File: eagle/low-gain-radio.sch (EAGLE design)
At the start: 132 parts, among them U1 MKW01Z128, U2 SKY65116, U3 W25Q80DV, U4 LP5907MFX-3.3, U6 LP5907MFX-3.3, U7 LD39200, U8 MAAL-010704, Y1 32MHz

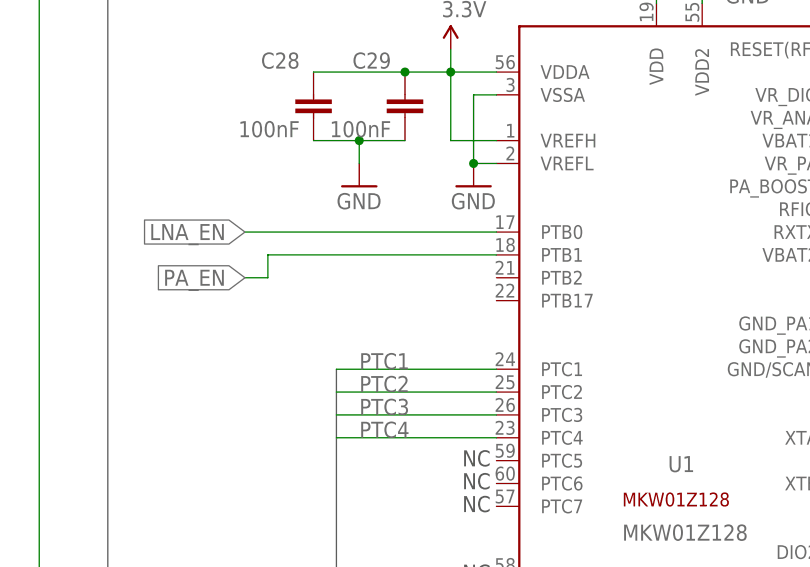
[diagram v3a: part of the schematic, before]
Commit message: added test points to PTB17, PTB2 and placed on PCB layout...also cleared a few stupid DRC errors on the PCB layout
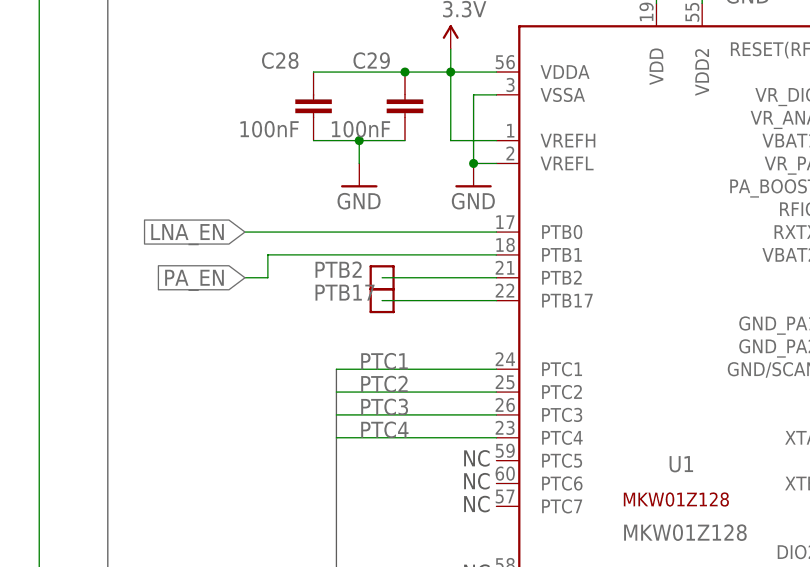
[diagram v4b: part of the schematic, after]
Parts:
- added PTB17, PTB2: TEST-POINT, Tova:TEST-POINT
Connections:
- new net PTB17: PTB17.1, U1.PTB17
- new net PTB2: PTB2.1, U1.PTB2
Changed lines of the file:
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@@
 <setting verticaltext="up"/>
 </settings>
-<grid distance="0.1" unitdist="inch" unit="inch" style="lines" multiple="1" display="yes" altdistance="0.01" altunitdist="inch" altunit="inch"/>
+<grid distance="0.1" unitdist="inch" unit="inch" style="lines" multiple="1" display="no" altdistance="0.01" altunitdist="inch" altunit="inch"/>
 <layers>
 <layer number="1" name="Top" color="4" fill="1" visible="no" active="no"/>
@@
 <attribute name="MPN" value="CBR04C101F3GAC"/>
 </part>
+<part name="PTB2" library="Tova" deviceset="TEST-POINT" device=""/>
+<part name="PTB17" library="Tova" deviceset="TEST-POINT" device=""/>
 </parts>
 <sheets>
@@
 <attribute name="MPN" x="530.86" y="190.5" size="1.778" layer="96" rot="R90" display="off"/>
 </instance>
+<instance part="PTB2" gate="G$1" x="81.28" y="220.98" smashed="yes">
+<attribute name="NAME" x="73.66" y="220.98" size="1.778" layer="95" font="vector"/>
+</instance>
+<instance part="PTB17" gate="G$1" x="81.28" y="218.44" smashed="yes">
+<attribute name="NAME" x="73.66" y="218.44" size="1.778" layer="95" font="vector"/>
+</instance>
 </instances>
 <busses>
@@
 </segment>
 </net>
+<net name="PTB2" class="0">
+<segment>
+<pinref part="U1" gate="G$1" pin="PTB2"/>
+<pinref part="PTB2" gate="G$1" pin="1"/>
+<wire x1="81.28" y1="220.98" x2="93.98" y2="220.98" width="0.1524" layer="91"/>
+</segment>
+</net>
+<net name="PTB17" class="0">
+<segment>
+<pinref part="U1" gate="G$1" pin="PTB17"/>
+<pinref part="PTB17" gate="G$1" pin="1"/>
+<wire x1="81.28" y1="218.44" x2="93.98" y2="218.44" width="0.1524" layer="91"/>
+</segment>
+</net>

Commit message: Big cleanup of v2_0 board. Includes changes to packages for LDOs and switch and reflectometer, ground stapling, adding a RGB LED, new board outline from rev 0.4 structure drawings, etc. Ready for production, except for possible switch to 0402s.
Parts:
- removed LED8: DNP/AMB, psas_c3_team05:LED-0603
- removed PTB17, PTB2: TEST-POINT, Tova:TEST-POINT
- removed U$22: BDCN-20-13+, low-gain-radio:BDCN-20-13+
- removed U$49: RF3025, low-gain-radio:RF3025
- added C59, C62: DNP, rcl_custom:C-EU0603-B-NOSILK
- added C63: 100pF, low-gain-radio:C-EU0402-C-NOSILK
- added LED9: SMLVN6RGB1W1, apdm:LED-RGB-SEPARATE-3528
- added R22, R23: DNP/1k, rcl_custom:R-US_0603-B-NOSILK
- added U5: RF3025, low-gain-radio:RF3025
- added U9: BDCN-20-13+, low-gain-radio:BDCN-20-13+
- added X0: DNP, microbuilder:CRYSTAL2.5X2.0MM
- added XTAL0: TEST-POINT, Tova:TEST-POINT
- renumbered XTAL to XTAL1, Y1 to X1
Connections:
- removed net DIO5/CLKOUT: DIO5/CLKOUT.1, U1.DIO5, U1.PTA18/EXTAL0
- new net EXTAL0: C62.2, DIO5/CLKOUT.1, U1.DIO5, U1.PTA18/EXTAL0, X0.1
- new net N$11: LED9B.K, R23.1
- new net N$26: LED9R.K, R12.1
- new net XTAL0: C59.2, U1.PTA19/XTAL0, X0.2, XTAL0.1
- net 3.3V: now also LED9B.A, LED9G.A, LED9R.A
- net DC_OUT: now also U9.OUT; no longer U$22.OUT
- net FWD: now also U9.FWD; no longer U$22.FWD
- net GND: now also C59.1, C62.1; no longer LED8.K
- net LNA_IN: now also U5.RF2; no longer U$49.RF2
- net N$23: now also LED9G.K, R22.1; no longer LED8.A, R12.1
- net PA_IN: now also U5.RF1; no longer U$49.RF1
- net PTA4/NMI_B: now also CF1.19, CF1.20; no longer CF1.2
- net PTB17: now also R23.2; no longer PTB17.1
- net PTB2: now also R22.2; no longer PTB2.1
- net REV: now also U9.REV; no longer U$22.REV
- net RFC: now also U9.IN; no longer U$22.IN
- net RF_GND: now also C63.1, U5.GND, U9.GND, U9.GND2; no longer U$22.GND, U$22.GND2, U$49.GND, U$49.GND1, U$49.GND10, U$49.GND2, U$49.GND3, U$49.GND4, U$49.GND5, U$49.GND6, U$49.GND7, U$49.GND8, U$49.GND9, U$49.PADDLE
- net RXTX: now also U5.VC; no longer U$49.VC
- net RXTX_OUT: now also U5.RFC; no longer U$49.RFC
- net UART0_RX: now also CF1.23, CF1.24; no longer CF1.17, CF1.18
- net UART0_TX: now also CF1.21, CF1.22; no longer CF1.15, CF1.16
- net VBIAS: now also C63.2, U5.VDD; no longer U$49.VDD
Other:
- note added: "CAN"
- note added: "MMCX to Antenna"
- note added: "Vpv"
- note removed: "GND lines for RF2 and RF3 need to go along their respective transmission lines to prevent intereference from other signals. I have left them this way though to conserve space."
- note removed: "MCX to 70 cm Antenna"
- moved on the sheet: C39, C40, C41, C42, C49, C52, C53, C55, C56, C57, C58, C60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

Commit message: did a sanity check everything looks good, added some missing attributes to parts on the schematic and changed some text on the board layout
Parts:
- LED9: DIST (none) -> Digi-Key Inc.; DPN (none) -> 846-1187-1-ND; MFG (none) -> Rohm Semiconductor; MPN (none) -> SMLVN6RGB1W1
- U2: DIST (none) -> Digi-Key Inc.; DPN (none) -> 863-1072-1-ND; MFG (none) -> Skyworks Solutions Inc.; MPN (none) -> SKY65116-21
- U5: DIST (none) -> Digi-Key Inc.; DPN (none) -> 689-1087-1-ND; MFG (none) -> RFMD; MPN (none) -> RF3025TR7
- U8: DIST (none) -> Digi-Key Inc.; DPN (none) -> 1465-1261-1-ND; MFG (none) -> M/A-Com Technology Solutions; MPN (none) -> MAAL-010704-TR3000
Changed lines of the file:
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@@
 <?xml version="1.0" encoding="utf-8"?>
 <!DOCTYPE eagle SYSTEM "eagle.dtd">
-<eagle version="7.5.0">
+<eagle version="7.3.0">
 <drawing>
 <settings>
@@
 <setting verticaltext="up"/>
 </settings>
-<grid distance="0.05" unitdist="inch" unit="inch" style="lines" multiple="1" display="no" altdistance="0.01" altunitdist="inch" altunit="inch"/>
+<grid distance="0.1" unitdist="inch" unit="inch" style="lines" multiple="1" display="no" altdistance="0.01" altunitdist="inch" altunit="inch"/>
 <layers>
 <layer number="1" name="Top" color="4" fill="1" visible="no" active="no"/>
@@
 <part name="DIO1" library="Tova" deviceset="TEST-POINT" device=""/>
 <part name="PG" library="Tova" deviceset="TEST-POINT" device=""/>
-<part name="U2" library="psas_c3_team05" deviceset="SKY65116" device=""/>
-<part name="U8" library="psas_c3_team05" deviceset="MAAL-010704" device=""/>
+<part name="U2" library="psas_c3_team05" deviceset="SKY65116" device="">
+<attribute name="DIST" value="Digi-Key Inc."/>
+<attribute name="DPN" value="863-1072-1-ND"/>
+<attribute name="MFG" value="
+Skyworks Solutions Inc."/>
+<attribute name="MPN" value="SKY65116-21"/>
+</part>
+<part name="U8" library="psas_c3_team05" deviceset="MAAL-010704" device="">
+<attribute name="DIST" value="Digi-Key Inc."/>
+<attribute name="DPN" value="1465-1261-1-ND"/>
+<attribute name="MFG" value="M/A-Com Technology Solutions"/>
+<attribute name="MPN" value="MAAL-010704-TR3000"/>
+</part>
 <part name="R13" library="rcl_custom" deviceset="R-US_" device="0603-B-NOSILK" value="DNP/0">
 <attribute name="DIST" value="Digi-Key"/>
@@
 <part name="GND3" library="psas_c3_team05" deviceset="GND" device=""/>
 <part name="XTAL0" library="Tova" deviceset="TEST-POINT" device=""/>
-<part name="LED9" library="apdm" deviceset="LED-RGB-SEPARATE-*" device="3528" value="SMLVN6RGB1W1"/>
+<part name="LED9" library="apdm" deviceset="LED-RGB-SEPARATE-*" device="3528" value="SMLVN6RGB1W1">
+<attribute name="DIST" value="Digi-Key Inc."/>
+<attribute name="DPN" value="846-1187-1-ND"/>
+<attribute name="MFG" value="Rohm Semiconductor"/>
+<attribute name="MPN" value="SMLVN6RGB1W1"/>
+</part>
 <part name="P+10" library="SparkFun-v5" deviceset="3.3V" device=""/>
 <part name="R12" library="rcl_custom" deviceset="R-US_" device="0603-B-NOSILK" value="DNP/1k">
@@
 <attribute name="MFG_PN" value="RC0603FR-071KL"/>
 </part>
-<part name="U5" library="low-gain-radio" deviceset="RF3025" device=""/>
+<part name="U5" library="low-gain-radio" deviceset="RF3025" device="">
+<attribute name="DIST" value="Digi-Key Inc."/>
+<attribute name="DPN" value="689-1087-1-ND"/>
+<attribute name="MFG" value="RFMD"/>
+<attribute name="MPN" value="RF3025TR7"/>
+</part>
 <part name="C63" library="low-gain-radio" deviceset="C-EU" device="0402-C-NOSILK" value="100pF">
 <attribute name="DIST" value="Digi-Key Inc."/>
@@
 <attribute name="NAME" x="392.43" y="266.7" size="1.778" layer="104" ratio="15"/>
 <attribute name="VALUE" x="392.43" y="264.16" size="1.778" layer="96"/>
+<attribute name="MFG" x="381" y="256.54" size="1.778" layer="96" display="off"/>
+<attribute name="MPN" x="381" y="256.54" size="1.778" layer="96" display="off"/>
+<attribute name="DIST" x="381" y="256.54" size="1.778" layer="96" display="off"/>
+<attribute name="DPN" x="381" y="256.54" size="1.778" layer="96" display="off"/>
 </instance>
 <instance part="U8" gate="G$1" x="381" y="147.32" smashed="yes">
 <attribute name="NAME" x="388.62" y="163.83" size="1.778" layer="104"/>
 <attribute name="VALUE" x="382.27" y="161.29" size="1.778" layer="96"/>
+<attribute name="MFG" x="381" y="147.32" size="1.778" layer="96" display="off"/>
+<attribute name="MPN" x="381" y="147.32" size="1.778" layer="96" display="off"/>
+<attribute name="DIST" x="381" y="147.32" size="1.778" layer="96" display="off"/>
+<attribute name="DPN" x="381" y="147.32" size="1.778" layer="96" display="off"/>
 </instance>
 <instance part="R13" gate="R" x="454.66" y="304.8" rot="R90">
@@
 <instance part="LED9" gate="G" x="220.98" y="20.32" smashed="yes" rot="R270">
 <attribute name="PART" x="229.87" y="17.78" size="1.778" layer="95" rot="R90"/>
+<attribute name="MFG" x="220.98" y="20.32" size="1.778" layer="96" rot="R270" display="off"/>
+<attribute name="MPN" x="220.98" y="20.32" size="1.778" layer="96" rot="R270" display="off"/>
+<attribute name="DIST" x="220.98" y="20.32" size="1.778" layer="96" rot="R270" display="off"/>
+<attribute name="DPN" x="220.98" y="20.32" size="1.778" layer="96" rot="R270" display="off"/>
 </instance>
 <instance part="LED9" gate="B" x="220.98" y="10.16" smashed="yes" rot="R270"/>
@@
 <attribute name="MFG_PN" x="208.28" y="10.16" size="1.778" layer="96" rot="R180" display="off"/>
 </instance>
-<instance part="U5" gate="G$1" x="477.52" y="190.5"/>
+<instance part="U5" gate="G$1" x="477.52" y="190.5">
+<attribute name="MFG" x="477.52" y="190.5" size="1.778" layer="96" display="off"/>
+<attribute name="MPN" x="477.52" y="190.5" size="1.778" layer="96" display="off"/>
+<attribute name="DIST" x="477.52" y="190.5" size="1.778" layer="96" display="off"/>
+<attribute name="DPN" x="477.52" y="190.5" size="1.778" layer="96" display="off"/>
+</instance>
 <instance part="C63" gate="CE" x="492.76" y="203.2" rot="R180">
 <attribute name="DIST" x="492.76" y="203.2" size="1.778" layer="96" rot="R180" display="off"/>

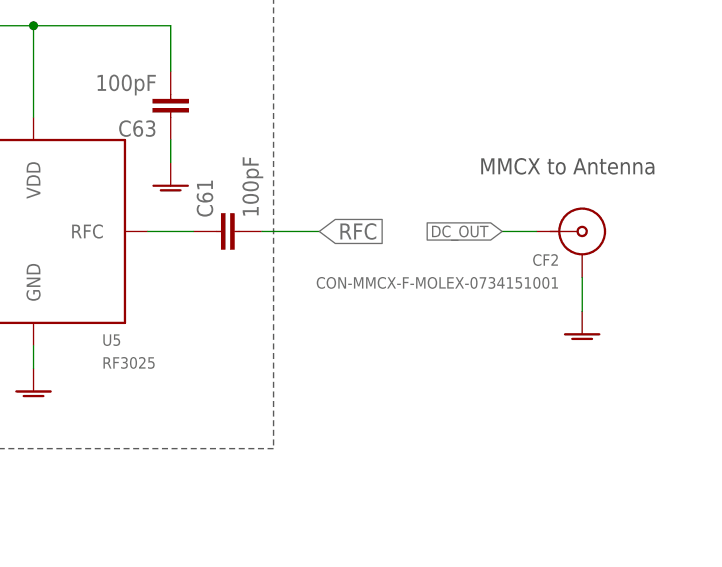
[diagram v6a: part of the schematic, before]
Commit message: Oh ugh. Didn't push my changes last night! Stupid human. Last night, I switched over most components to 0402s that made sense. Kept 0603 for some larger components, like 1uF or larger caps and a power resistor. Will updated some this morning, which weren't on the 0402 switch over. Pulled, and tried to rescue Will's changes: updated text, added attribs.
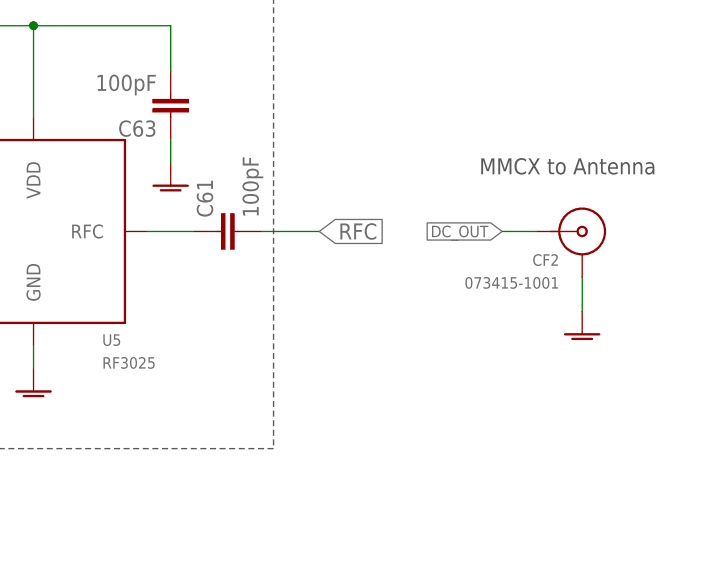
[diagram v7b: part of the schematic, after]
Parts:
- C1, C10, C11, C12, C14, C16, C18, C2, C20, C21, C26, C27, C28, C29, C3, C30, C31, C32, C33, C34, C35, C37, C4, C40, C42, C45, C47, C48, C5, C59, C6, C62, C7, C8, C9: device rcl_custom:C-EU0603-B-NOSILK -> low-gain-radio:C-EU0402-B-NOSILK
- C23, C49, C55, C56, C57, C58, C60, C61, C63: device low-gain-radio:C-EU0402-C-NOSILK -> low-gain-radio:C-EU0402-B-NOSILK
- C24, C44, C50, C51, C54: device rcl_custom:C-EU0402-B-NOSILK -> low-gain-radio:C-EU0402-B-NOSILK
- CF2: value CON-MMCX-F-MOLEX-0734151001 -> 073415-1001; DIST (none) -> Digi-Key; DPN (none) -> WM5552-ND; MFN (none) -> Molex; MPN (none) -> 073415-1001
- L1, L2, L3, L4, L5, L6, L8: device rcl_custom:L-US0603-B-NOSILK -> low-gain-radio:L-US0402-B-NOSILK
- LED9: DIST Digi-Key Inc. -> Digi-Key; MFG Rohm Semiconductor -> (none); MFN (none) -> Rohm
- R10, R11, R12, R13, R14, R2, R22, R23, R3, R4, R5, R6, R7, R8, R9: device rcl_custom:R-US_0603-B-NOSILK -> low-gain-radio:R-US_0402-B-NOSILK
- R18, R19, R20, R21: device low-gain-radio:R-US_0402-C-NOSILK -> low-gain-radio:R-US_0402-B-NOSILK
- U2: DIST Digi-Key Inc. -> Digi-Key; MFG Skyworks Solutions Inc. -> (none); MFN (none) -> Skyworks
- U5: DIST Digi-Key Inc. -> Digi-Key; MFG RFMD -> (none); MFN (none) -> RFMD
- U8: DIST Digi-Key Inc. -> Digi-Key; MFG M/A-Com Technology Solutions -> (none); MFN (none) -> M/A-Com

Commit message: Updated BOM, and schematic values afterwards. Lots to cleanup!
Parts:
- C1, C16, C18, C20, C21, C3, C37, C40: MFG_PN GRM188R71H103KA01D -> (none); MPN (none) -> GRM188R71H103KA01D
- C10, C5, C6, C9: MFG_PN GRM1885C1H150JA01D -> (none); MPN (none) -> GRM1885C1H150JA01D
- C11, C12: MFG_PN 06031U8R2BAT2A -> (none); MPN (none) -> 06031U8R2BAT2A
- C13, C15, C17, C19, C22, C38, C41, C46: MFG_PN GRM188R60J106ME47J -> (none); MPN (none) -> GRM188R60J106ME47J
- C14: value 100nF -> 100pF; MFG_PN 06035C104JAT2A -> (none); MPN (none) -> 06035C104JAT2A
- C2, C4: MFG_PN GRM1885C1H120JA01D -> (none); MPN (none) -> GRM1885C1H120JA01D
- C23, C49, C55, C56, C57, C58, C60, C61, C63, D1, D2, R15, R16, R17, R18, R19: DIST Digi-Key Inc. -> Digi-Key
- C24, C54: MFG_PN GRM155R71H102KA01D -> (none); MPN (none) -> GRM155R71H102KA01D
- C25: value 1nF -> 100pF; MFG_PN GRM155R71H102KA01D -> (none); MPN (none) -> GRM155R71H102KA01D
- C26, C27, C28, C29, C30, C31, C32, C33, C42, C48: MFG_PN 06035C104JAT2A -> (none); MPN (none) -> 06035C104JAT2A
- C34, C35: MFG_PN GQM1875C2E6R0BB12D -> (none); MPN (none) -> GQM1875C2E6R0BB12D
- C36, C39: MFG_PN GRM188R61A105KA61D -> (none); MPN (none) -> GRM188R61A105KA61D
- C43: MFG_PN TAJC107K010RNJ -> (none); MPN (none) -> TAJC107K010RNJ
- C44: MFG_PN GRM155R71H103KA88D -> (none); MPN (none) -> GRM155R71H103KA88D
- C45, C47: value 100nF -> 0K/100nF; MFG_PN 06035C104JAT2A -> (none); MPN (none) -> 06035C104JAT2A
- C50, C51: value 10nF -> 0K/10nF; MFG_PN GRM155R71H102KA01D -> (none); MPN (none) -> GRM155R71H102KA01D
- C53: value 10 uF -> 10uF; MFG_PN GRM188R60J106ME47J -> (none); MPN (none) -> GRM188R60J106ME47J
- C59, C62: value DNP -> DNP/6pF; MFG_PN GQM1875C2E6R0BB12D -> (none); MPN (none) -> GQM1875C2E6R0BB12D
- C64: value 10 uF -> 10uF; DIST (none) -> Digi-Key; DPN (none) -> 490-6405-2-ND; MFG (none) -> Murata; MPN (none) -> GRM188R60J106ME47J
- C7, C8: MFG_PN GRM1885C1H2R2CA01D -> (none); MPN (none) -> GRM1885C1H2R2CA01D
- CF1: DIST (none) -> Digi-Key; DPN (none) -> 952-1381-5-ND; MFG (none) -> Harwin Archer; MPN (none) -> M50-3202045
- CF2: MFG (none) -> Molex; MFN Molex -> (none)
- CM1: value 3220-10-0100-00 -> 3221-10-0200-00; device low-gain-radio:JTAG_ARM-10-50MIL -> low-gain-radio:JTAG_ARM-10-; DPN 1175-1627-ND -> 1175-1734-ND; MFG_PN 3220-10-0100-00 -> (none); MPN (none) -> 3221-10-0200-00
- CM2: DIST (none) -> Digi-Key; DPN (none) -> 609-3316-ND; MFN (none) -> Amphenol; MPN (none) -> 68016-112HLF
- L1, L2: MFG_PN LQW18AN22NG00D -> (none); MPN (none) -> LQW18AN22NG00D
- L3, L4, L5, L6: MFG_PN LQW18AN15NG00D -> (none); MPN (none) -> LQW18AN15NG00D
- L8: MFG_PN LQW18AN82NG00D -> (none); MPN (none) -> LQW18AN82NG00D
- LED1, LED2, LED3, LED4: MFG_PN LTST-C191KGKT -> (none); MPN (none) -> LTST-C191KGKT
- LED5, LED6, LED7: MFG_PN LTST-C191AKT -> (none); MPN (none) -> LTST-C191AKT
- LED9: MFG (none) -> Rohm; MFN Rohm -> (none)
- R1: MFG_PN RC1608F2490CS -> (none); MPN (none) -> RC1608F2490CS
- R10, R11, R12, R22, R23, R4, R6, R7, R8, R9: MFG_PN RC0603FR-071KL -> (none); MPN (none) -> RC0603FR-071KL
- R13, R14: MFG_PN RC0603JR-070RL -> (none); MPN (none) -> RC0603JR-070RL
- R2, R3, R5: MFG_PN RC0603FR-0710KL -> (none); MPN (none) -> RC0603FR-0710KL
- R20, R21: value 20k -> 4.7k; DIST Digi-Key Inc. -> Digi-Key
- U1: MFG (none) -> NXP; MFN NXP -> (none)
- U2: MFG (none) -> Skyworks; MFN Skyworks -> (none)
- U3: MFG_PN W25Q80DVSSIG -> (none); MPN (none) -> W25Q80DVSSIG
- U4, U6: MFG (none) -> Texas Instruments; MFN Texas Instruments -> (none); MFN-PN LP5907MFX-3.3 -> (none); MPN (none) -> LP5907MFX-3.3
- U5: MFG (none) -> RFMD; MFN RFMD -> (none)
- U7: MFG_PN LD39200PU33R -> (none); MPN (none) -> LD39200PU33R
- U8: MFG (none) -> M/A-Com; MFN M/A-Com -> (none)
- X0: value DNP -> DNP/16 MHz; MFG (none) -> EPSON; MFN EPSON -> (none)
- X1: MFG (none) -> EPSON; MFN EPSON -> (none)
- renumbered C52 to C64
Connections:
- removed net DC_OUT: CF2.CENTER, U9.OUT
- removed net N$25: C23.1, U8.RFIN
- removed net RFC: C61.2, U9.IN
- removed net RFOUT: C58.1, U2.RFOUT
- new net LNA_IN_DC: C23.2, U5.RF2
- new net N$29: C58.1, U9.OUT
- new net N$30: C61.2, CF2.CENTER
- new net PA-OUT: U2.RFOUT, U9.IN
- net LNA_IN: now also C23.1, U8.RFIN; no longer C23.2, U5.RF2
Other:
- note added: "0805"
- note added: "2.0"
- note added: "= 3.3V"
- note added: "All capacitors are X5R 10% Vw>=10V 0402 unless noted."
- note added: "All resistors are 1% 0402 unless noted."
- note added: "Replace Caps with 0 ohm 0402 resistors for flight."
- note added: "SHIELD"
- note added: "WARNING: RLC ATTRIBUTES ARE NOT CORRECT"
- note removed: "= 3.0V"
- moved on the sheet: C1, C11, C13, C14, C15, C16, C17, C18, C19, C2, C20, C21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
